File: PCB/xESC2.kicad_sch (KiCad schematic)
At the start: 31 parts, among them J1 Conn_01x09_Male, J2 U254-051T-4BH83-F1S, J3 Conn_01x05_Male, J4 Conn_01x05_Male

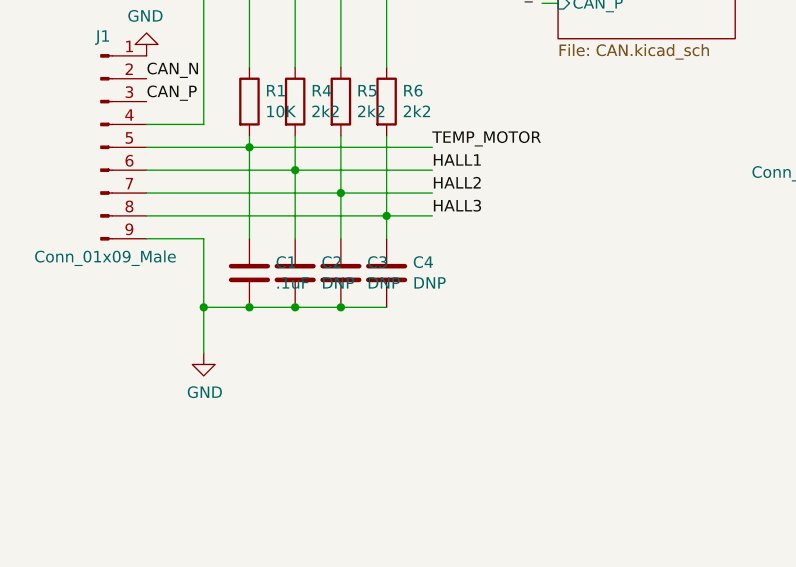
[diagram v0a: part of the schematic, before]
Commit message: added .1uF for C2-C4
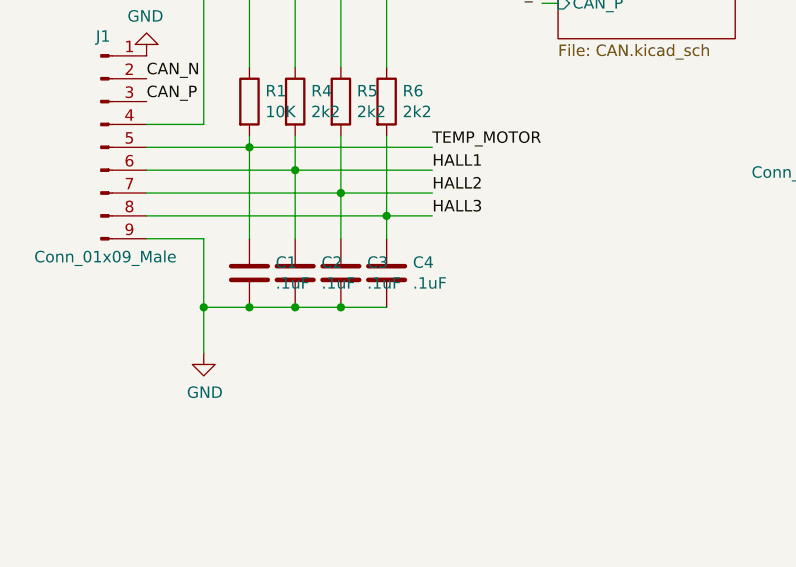
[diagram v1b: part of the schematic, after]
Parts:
- C2, C3, C4: value DNP -> .1uF; Config do not place -> (none); Digikey (none) -> 1276-1935-1-ND; Part Number (none) -> CL10B104KC8NNNC; Stock_PN (none) -> C-603-.1uF-100V-X7R
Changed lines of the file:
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@@
       (effects (font (size 1.27 1.27)) (justify left))
     )
-    (property "Value" "DNP" (id 1) (at 54.991 128.143 0)
+    (property "Value" ".1uF" (id 1) (at 54.991 128.143 0)
       (effects (font (size 1.27 1.27)) (justify left))
     )
@@
       (effects (font (size 1.27 1.27)) hide)
     )
-    (property "Config" "do not place" (id 4) (at 52.07 127 0)
+    (property "Config" "" (id 4) (at 52.07 127 0)
+      (effects (font (size 1.27 1.27)) hide)
+    )
+    (property "Digikey" "1276-1935-1-ND" (id 5) (at 52.07 127 0)
+      (effects (font (size 1.27 1.27)) hide)
+    )
+    (property "Part Number" "CL10B104KC8NNNC" (id 6) (at 52.07 127 0)
+      (effects (font (size 1.27 1.27)) hide)
+    )
+    (property "Stock_PN" "C-603-.1uF-100V-X7R" (id 7) (at 52.07 127 0)
       (effects (font (size 1.27 1.27)) hide)
     )
@@
       (effects (font (size 1.27 1.27)) (justify left))
     )
-    (property "Value" "DNP" (id 1) (at 49.911 128.143 0)
+    (property "Value" ".1uF" (id 1) (at 49.911 128.143 0)
       (effects (font (size 1.27 1.27)) (justify left))
     )
@@
       (effects (font (size 1.27 1.27)) hide)
     )
-    (property "Config" "do not place" (id 4) (at 46.99 127 0)
+    (property "Config" "" (id 4) (at 46.99 127 0)
+      (effects (font (size 1.27 1.27)) hide)
+    )
+    (property "Digikey" "1276-1935-1-ND" (id 5) (at 46.99 127 0)
+      (effects (font (size 1.27 1.27)) hide)
+    )
+    (property "Part Number" "CL10B104KC8NNNC" (id 6) (at 46.99 127 0)
+      (effects (font (size 1.27 1.27)) hide)
+    )
+    (property "Stock_PN" "C-603-.1uF-100V-X7R" (id 7) (at 46.99 127 0)
       (effects (font (size 1.27 1.27)) hide)
     )
@@
       (effects (font (size 1.27 1.27)) (justify left))
     )
-    (property "Value" "DNP" (id 1) (at 44.831 128.143 0)
+    (property "Value" ".1uF" (id 1) (at 44.831 128.143 0)
       (effects (font (size 1.27 1.27)) (justify left))
     )
@@
       (effects (font (size 1.27 1.27)) hide)
     )
-    (property "Config" "do not place" (id 4) (at 41.91 127 0)
+    (property "Config" "" (id 4) (at 41.91 127 0)
+      (effects (font (size 1.27 1.27)) hide)
+    )
+    (property "Digikey" "1276-1935-1-ND" (id 5) (at 41.91 127 0)
+      (effects (font (size 1.27 1.27)) hide)
+    )
+    (property "Part Number" "CL10B104KC8NNNC" (id 6) (at 41.91 127 0)
+      (effects (font (size 1.27 1.27)) hide)
+    )
+    (property "Stock_PN" "C-603-.1uF-100V-X7R" (id 7) (at 41.91 127 0)
       (effects (font (size 1.27 1.27)) hide)
     )
@@
     )
     (path "/00000000-0000-0000-0000-000061b68b12"
-      (reference "C2") (unit 1) (value "DNP") (footprint "Capacitor_SMD:C_0603_1608Metric")
+      (reference "C2") (unit 1) (value ".1uF") (footprint "Capacitor_SMD:C_0603_1608Metric")
     )
     (path "/00000000-0000-0000-0000-000061b63c43"
-      (reference "C3") (unit 1) (value "DNP") (footprint "Capacitor_SMD:C_0603_1608Metric")
+      (reference "C3") (unit 1) (value ".1uF") (footprint "Capacitor_SMD:C_0603_1608Metric")
     )
     (path "/00000000-0000-0000-0000-000061b5ed85"
-      (reference "C4") (unit 1) (value "DNP") (footprint "Capacitor_SMD:C_0603_1608Metric")
+      (reference "C4") (unit 1) (value ".1uF") (footprint "Capacitor_SMD:C_0603_1608Metric")
     )
     (path "/00000000-0000-0000-0000-000061ac26fb/917ece1c-a193-4495-95d8-fbf522672114"
